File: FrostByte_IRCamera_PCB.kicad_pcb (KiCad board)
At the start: 2 copper layers, 43 parts, among them J1 Conn_01x04_Socket, J4 Conn_01x04_Socket, J5 Power_Input, J6 Conn_02x10, J7 Conn_01x02_Socket, Q1 SI3127DV-T1-GE3, SW1 SW_Push, SW2 SW_Push, U1 AP63203WU-7, U2 ESP32-S3-WROOM-1, Y2 32.768kHz

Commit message: Schematic + Layout Review Ready First Rev
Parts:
- removed D5: LED_Blue, LED_SMD:LED_0805_2012Metric_Pad1.15x1.40mm_HandSolder
- removed D6: LED_Green, LED_SMD:LED_0805_2012Metric_Pad1.15x1.40mm_HandSolder
- removed J6: Conn_02x10, Connector_PinHeader_2.54mm:PinHeader_2x10_P2.54mm_Vertical
- removed J7: Conn_01x02_Socket, TerminalBlock:TerminalBlock_Xinya_XY308-2.54-2P_1x02_P2.54mm_Horizontal
- removed L2: 6.8uH, footprints:IND_VLS6045EX-6R8M
- removed Y2: 32.768kHz, footprints:XTAL_FC-135R_32.7680KA-AG0
- added 2V8: TestPoint, TestPoint:TestPoint_THTPad_1.5x1.5mm_Drill0.7mm, F.Cu at (146.5, 132.5)
- added 3.3V: TestPoint, TestPoint:TestPoint_THTPad_1.5x1.5mm_Drill0.7mm, F.Cu at (150.5, 132.5)
- added C1: 47uF, Capacitor_THT:CP_Radial_D5.0mm_P2.00mm, F.Cu at (193.5, 129.5)
- added C12: 8pF, Capacitor_SMD:C_0805_2012Metric_Pad1.18x1.45mm_HandSolder, F.Cu at (160.5, 99.0)
- added C13: 22uF, Capacitor_SMD:C_1206_3216Metric_Pad1.33x1.80mm_HandSolder, F.Cu at (163.0, 86.0)
- added C16: 0.1uF, Capacitor_SMD:C_0805_2012Metric_Pad1.18x1.45mm_HandSolder, F.Cu at (176.5, 125.5)
- added CLK: TestPoint, TestPoint:TestPoint_THTPad_1.5x1.5mm_Drill0.7mm, F.Cu at (151.0, 115.5)
- added CS: TestPoint, TestPoint:TestPoint_THTPad_1.5x1.5mm_Drill0.7mm, F.Cu at (156.5, 115.5)
- added D2: LED_Red, LED_SMD:LED_0805_2012Metric_Pad1.15x1.40mm_HandSolder, F.Cu at (191.5, 139.0)
- added D3: LED_Blue, LED_SMD:LED_0805_2012Metric_Pad1.15x1.40mm_HandSolder, F.Cu at (196.0, 98.5)
- added GND: TestPoint, TestPoint:TestPoint_THTPad_1.5x1.5mm_Drill0.7mm, F.Cu at (154.5, 132.5)
- added J2: Conn_01x02_Socket, TerminalBlock:TerminalBlock_Xinya_XY308-2.54-2P_1x02_P2.54mm_Horizontal, F.Cu at (148.0, 88.0)
- added J3: Conn_01x04_Socket, Connector_JST:JST_SH_BM04B-SRSS-TB_1x04-1MP_P1.00mm_Vertical, F.Cu at (150.5, 139.5)
- added L1: 3.9uH, footprints:IND_VLS6045EX-6R8M, F.Cu at (185.5, 118.5)
- added MISO: TestPoint, TestPoint:TestPoint_THTPad_1.5x1.5mm_Drill0.7mm, F.Cu at (156.5, 121.5)
- added MOSI: TestPoint, TestPoint:TestPoint_THTPad_1.5x1.5mm_Drill0.7mm, F.Cu at (151.0, 121.5)
- added R10: 47, Resistor_SMD:R_0805_2012Metric_Pad1.20x1.40mm_HandSolder, F.Cu at (200.5, 98.5)
- added R14: 33, Resistor_SMD:R_0805_2012Metric_Pad1.20x1.40mm_HandSolder, F.Cu at (165.0, 112.0)
- added R2: 10k 1%, Resistor_SMD:R_0805_2012Metric_Pad1.20x1.40mm_HandSolder, F.Cu at (144.5, 95.5)
- added R5: 10k, Resistor_SMD:R_0805_2012Metric_Pad1.20x1.40mm_HandSolder, F.Cu at (167.5, 130.5)
- added R6: 2.2k, Resistor_SMD:R_0805_2012Metric_Pad1.20x1.40mm_HandSolder, F.Cu at (167.0, 106.5)
- added R9: 10k, Resistor_SMD:R_0805_2012Metric_Pad1.20x1.40mm_HandSolder, F.Cu at (188.0, 108.0)
- added RX: TestPoint, TestPoint:TestPoint_THTPad_1.5x1.5mm_Drill0.7mm, F.Cu at (196.0, 89.0)
- added SCL: TestPoint, TestPoint:TestPoint_THTPad_1.5x1.5mm_Drill0.7mm, F.Cu at (151.0, 107.0)
- added SDA: TestPoint, TestPoint:TestPoint_THTPad_1.5x1.5mm_Drill0.7mm, F.Cu at (151.0, 102.5)
- added TX: TestPoint, TestPoint:TestPoint_THTPad_1.5x1.5mm_Drill0.7mm, F.Cu at (200.5, 89.0)
- added U3: SN74AXC4T245PWR, footprints:SOP65P640X120-16N, F.Cu at (175.5, 117.5)
- added Y1: 32.768kHz, footprints:XTAL_FC-135R_32.7680KA-AG0, F.Cu at (165.5, 96.8)
- C10: value 2.2uF -> 0.1uF
- C11: value 0.1uF -> 8pF
- C14, C15, C8: value 22uF -> 0.1uF; footprint Capacitor_SMD:C_1206_3216Metric_Pad1.33x1.80mm_HandSolder -> Capacitor_SMD:C_0805_2012Metric_Pad1.18x1.45mm_HandSolder
- C2: value 0.1uF -> 2.2uF
- C4: value 47uF -> 22uF; footprint Capacitor_THT:CP_Radial_D5.0mm_P2.00mm -> Capacitor_SMD:C_1206_3216Metric_Pad1.33x1.80mm_HandSolder
- C5: value 8pF -> 22uF; footprint Capacitor_SMD:C_0805_2012Metric_Pad1.18x1.45mm_HandSolder -> Capacitor_SMD:C_1206_3216Metric_Pad1.33x1.80mm_HandSolder
- C7: value 8pF -> 1uF
- D1: value SMAJ30A -> SMAJ33A
- D4: value LED_Red -> LED_Green
- J1: value Conn_01x04_Socket -> Power_Input; footprint Connector_PinSocket_2.54mm:PinSocket_1x04_P2.54mm_Vertical -> TerminalBlock:TerminalBlock_Xinya_XY308-2.54-2P_1x02_P2.54mm_Horizontal
- J4: value Conn_01x04_Socket -> Conn_02x10; footprint Connector_JST:JST_SH_BM04B-SRSS-TB_1x04-1MP_P1.00mm_Vertical -> Connector_PinHeader_2.54mm:PinHeader_2x10_P2.54mm_Vertical
- J5: value Power_Input -> Conn_01x04_Socket; footprint TerminalBlock:TerminalBlock_Xinya_XY308-2.54-2P_1x02_P2.54mm_Horizontal -> Connector_PinSocket_2.54mm:PinSocket_1x04_P2.54mm_Vertical
- R1: value 10k -> 100k
- R11: value 270 -> 150
- R12: value 47 -> 22
- R13: value 150 -> 22
- R4: value 100k -> 2.2k
- R7: value 10k 1% -> 22
- R8: value 10k -> 270
- moved J4 80.1 mm to (136.0, 102.4), turned to 0 degrees
- moved J1 67.8 mm to (215.5, 129.0)
- moved C6 48.0 mm to (149.0, 95.5)
- moved G*** 47.5 mm to (206.0, 106.0)
- moved C11 47.0 mm to (160.5, 94.5), turned to 0 degrees
- moved C14 42.7 mm to (168.0, 86.0), turned to 180 degrees
- moved C5 41.9 mm to (182.5, 126.0), turned to -90 degrees
- moved R1 41.1 mm to (208.5, 122.5), turned to 180 degrees
- moved J5 40.1 mm to (207.0, 90.4), turned to 0 degrees
- moved C15 40.1 mm to (172.5, 125.5), turned to -90 degrees
- moved R8 38.8 mm to (186.0, 139.0), turned to 0 degrees
- moved C9 38.2 mm to (172.5, 130.5), turned to -90 degrees
- moved R13 37.4 mm to (165.0, 116.0), turned to 0 degrees
- moved R12 36.8 mm to (165.0, 120.0), turned to 0 degrees
- moved R4 36.3 mm to (171.5, 108.0), turned to 90 degrees
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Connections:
- C10 pad 1: Net-(U1-EN) -> GND
- C10 pad 2: GND -> Net-(U2-EN)
- C11 pad 1: Net-(U1-BST) -> GND
- C11 pad 2: Net-(U1-SW) -> Net-(U2-IO15)
- C2 pad 1: GND -> Net-(U1-EN)
- C2 pad 2: Net-(U2-EN) -> GND
- C3 pad 1: GND -> Net-(U1-BST)
- C3 pad 2: Net-(U2-IO0) -> Net-(U1-SW)
- C4 pad 1: Net-(U1-EN) -> +3.3V
- C5 pad 1: GND -> +3.3V
- C5 pad 2: Net-(U2-IO15) -> GND
- C7 pad 1: GND -> +3.3V
- C7 pad 2: Net-(U2-IO16) -> GND
- C8 pad 1: +3.3V -> +2V8
- C9 pad 1: +3.3V -> GND
- C9 pad 2: GND -> Net-(U2-IO0)
- D4 pad 1: GND -> /MCU/LED_2
- F1 pad 1: LINE -> Net-(J1-Pin_1)
- J1 pad 1: +3.3V -> Net-(J1-Pin_1)
- J1 pad 2: /MCU/TX -> GND
- J4 pad 1: /Peripherals/SCL -> GND
- J4 pad 2: /Peripherals/SDA -> +3.3V
- J4 pad 3: +3.3V -> unconnected-(J4-Pin_3-Pad3)
- J4 pad 4: GND -> unconnected-(J4-Pin_4-Pad4)
- J5 pad 1: LINE -> +3.3V
- J5 pad 2: GND -> /MCU/TX
- R1 pad 1: +3.3V -> GND
- R1 pad 2: /Peripherals/SCL -> Net-(Q1-Pad3)
- R12 pad 1: +3.3V -> /MCU/SPI_CS
- R13 pad 1: +3.3V -> /MCU/SPI_MOSI
- R3 pad 1: Net-(U2-EN) -> Net-(J4-Pin_20)
- R3 pad 2: +3.3V -> +2V8
- R4 pad 1: GND -> +2V8
- R4 pad 2: Net-(Q1-Pad3) -> /Peripherals/SCL
- R7 pad 1: +3.3V -> Net-(U2-IO13)
- R7 pad 2: /MCU/CAM_TEMP -> /MCU/SPI_MISO
- R8 pad 2: /Peripherals/SDA -> Net-(D2-A)
- SW1 pad 2: Net-(U2-EN) -> Net-(U2-IO0)
- SW2 pad 2: Net-(U2-IO0) -> Net-(U2-EN)
- U2 pad 18: /MCU/SPI_CS -> /MCU/SPI_CS_3v3
- U2 pad 19: /MCU/SPI_MOSI -> /MCU/SPI_MOSI_3v3
- U2 pad 20: /MCU/SPI_CLK -> /MCU/SPI_CLK_3v3
- U2 pad 21: /MCU/SPI_MISO -> Net-(U2-IO13)
- U2 pad 23: unconnected-(U2-IO21-Pad23) -> /MCU/VSYNC
- U2 pad 25: /MCU/CAM_TEMP -> unconnected-(U2-IO48-Pad25)
- U2 pad 26: unconnected-(U2-IO45-Pad26) -> /MCU/RESET_L_3v3
- U2 pad 33: /MCU/VSYNC -> unconnected-(U2-IO40-Pad33)
- U2 pad 34: /MCU/RESET_L -> unconnected-(U2-IO41-Pad34)
- U2 pad 35: /MCU/PW_DWN_L -> unconnected-(U2-IO42-Pad35)
- U2 pad 4: unconnected-(U2-IO4-Pad4) -> /MCU/CAM_TEMP
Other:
- copper layers 2 -> 4
- board text added: "IR Camera Interface PCB Domenic Hampson"

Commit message: rev 2 added usb prog and i2c level shifting
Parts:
- added D5: 15V, footprints:DIOM5226X240N, F.Cu at (208.5, 117.5)
- moved G*** 1.00 mm to (206.0, 107.0)
- moved J5 0.50 mm to (206.5, 90.4)
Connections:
- D1 pad 1: Net-(D1-A1) -> /Power_Circuitry/source
- F1 pad 2: Net-(D1-A1) -> /Power_Circuitry/source
- J4 pad 10: /MCU/SPI_CS -> /MCU/SPI_MISO
- J4 pad 11: unconnected-(J4-Pin_11-Pad11) -> /MCU/SPI_MOSI
- J4 pad 12: /MCU/SPI_MISO -> /MCU/SPI_CS
- J4 pad 13: unconnected-(J4-Pin_13-Pad13) -> /MCU/SPI_CLK
- J4 pad 14: unconnected-(J4-Pin_14-Pad14) -> /Peripherals/SCL
- J4 pad 15: /MCU/VSYNC -> /Peripherals/SDA
- J4 pad 16: unconnected-(J4-Pin_16-Pad16) -> +2V8
- J4 pad 17: /MCU/RESET_L -> unconnected-(J4-Pin_17-Pad17)
- J4 pad 2: +3.3V -> Net-(J4-Pin_2)
- J4 pad 20: Net-(J4-Pin_20) -> +3.3V
- J4 pad 3: unconnected-(J4-Pin_3-Pad3) -> /MCU/RESET_L
- J4 pad 5: /Peripherals/SDA -> /MCU/VSYNC
- J4 pad 6: +2V8 -> unconnected-(J4-Pin_6-Pad6)
- J4 pad 7: /MCU/SPI_CLK -> unconnected-(J4-Pin_7-Pad7)
- J4 pad 8: /Peripherals/SCL -> unconnected-(J4-Pin_8-Pad8)
- J4 pad 9: /MCU/SPI_MOSI -> unconnected-(J4-Pin_9-Pad9)
- Q1 pad 1: Net-(D1-A1) -> /Power_Circuitry/source
- Q1 pad 2: unconnected-(Q1-Pad2) -> /Power_Circuitry/source
- Q1 pad 5: unconnected-(Q1-Pad5) -> /Power_Circuitry/source
- Q1 pad 6: unconnected-(Q1-Pad6) -> /Power_Circuitry/source
- R3 pad 1: Net-(J4-Pin_20) -> Net-(J4-Pin_2)
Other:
- board text added: "3V3"
- board text added: "3v3"
- board text added: "GND"
- board text removed: "1 (needs to be here)"

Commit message: minor fixes and updated PCB layout
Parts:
- removed 2V8, 3.3V: TestPoint, TestPoint:TestPoint_THTPad_1.5x1.5mm_Drill0.7mm
- removed the G*** at (206.0, 107.0)
- added 2v8: TestPoint, TestPoint:TestPoint_THTPad_1.5x1.5mm_Drill0.7mm, F.Cu at (197.0, 141.0)
- added 3v3: TestPoint, TestPoint:TestPoint_THTPad_1.5x1.5mm_Drill0.7mm, F.Cu at (202.0, 141.0)
- added C17: 0.1uF, Capacitor_SMD:C_0805_2012Metric_Pad1.18x1.45mm_HandSolder, F.Cu at (153.0, 109.0)
- added C18: 0.1uF, Capacitor_SMD:C_0805_2012Metric_Pad1.18x1.45mm_HandSolder, F.Cu at (167.0, 111.0)
- added C19: 0.1uF, Capacitor_SMD:C_0805_2012Metric_Pad1.18x1.45mm_HandSolder, F.Cu at (206.0, 112.0)
- added D6: SS34, footprints:DIO_SS34, F.Cu at (202.0, 106.0)
- added F2: 3A, Fuse:Fuse_0603_1608Metric_Pad1.05x0.95mm_HandSolder, F.Cu at (198.0, 113.0)
- added G***: LOGO, footprints:Small_Logo, F.Cu at (152.0, 116.0)
- added J6: GSB1C41110SSHR, footprints:AMPHENOL_GSB1C41110SSHR, F.Cu at (218.6, 101.1)
- added R15: 22, Resistor_SMD:R_0805_2012Metric_Pad1.20x1.40mm_HandSolder, F.Cu at (211.0, 103.0)
- added R16: 5.1k, Resistor_SMD:R_0805_2012Metric_Pad1.20x1.40mm_HandSolder, F.Cu at (211.0, 107.0)
- added R17: 10k, Resistor_SMD:R_0805_2012Metric_Pad1.20x1.40mm_HandSolder, F.Cu at (195.0, 103.0)
- added R18: 0, Resistor_SMD:R_0805_2012Metric_Pad1.20x1.40mm_HandSolder, F.Cu at (192.0, 109.0)
- added U4: TCA9517DGKR, footprints:SOP65P490X110-8N, F.Cu at (160.0, 109.0)
- C13: value 22uF -> DNP
- J3: footprint Connector_JST:JST_SH_BM04B-SRSS-TB_1x04-1MP_P1.00mm_Vertical -> footprints:CONN4_BM04B-SRSS_JST
- J5: value Conn_01x04_Socket -> UART; footprint Connector_PinSocket_2.54mm:PinSocket_1x04_P2.54mm_Vertical -> footprints:CONN4_BM04B-SRSS_JST
- moved GND 53.2 mm to (207.0, 141.0)
- moved R7 30.8 mm to (211.0, 99.0), turned to 180 degrees
- moved CLK 19.7 mm to (142.0, 133.0)
- moved CS 18.7 mm to (150.0, 133.0)
- moved MOSI 12.5 mm to (146.0, 133.0)
- moved MISO 11.8 mm to (154.0, 133.0)
- moved SCL 11.4 mm to (154.0, 96.0)
- moved RX 5.39 mm to (201.0, 87.0)
- moved R12 4.12 mm to (166.0, 124.0)
- moved R13 4.12 mm to (166.0, 120.0)
- moved R14 4.12 mm to (166.0, 116.0)
- moved TX 4.03 mm to (197.0, 87.0)
- moved SDA 3.35 mm to (154.0, 101.0)
- moved R6 1.50 mm to (167.0, 105.0)
- moved U3 1.50 mm to (175.5, 119.0)
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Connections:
- C9 pad 2: Net-(U2-IO0) -> Net-(C9-Pad2)
- D5 pad 1: Net-(D5-K) -> /Power_Circuitry/source
- D5 pad 2: /Power_Circuitry/source -> Net-(D5-A)
- J3 pad 1: /Peripherals/SCL -> /MCU/SCL_A
- J3 pad 2: /Peripherals/SDA -> /MCU/SDA_A
- J4 pad 14: /Peripherals/SCL -> /MCU/SCL_B
- J4 pad 15: /Peripherals/SDA -> /MCU/SDA_B
- J5 pad 1: +3.3V -> +5V
- J5 pad 2: /MCU/TX -> /MCU/RX
- J5 pad 3: /MCU/RX -> /MCU/TX
- Q1 pad 3: Net-(D5-K) -> Net-(D5-A)
- R1 pad 2: Net-(D5-K) -> Net-(D5-A)
- R4 pad 1: +2V8 -> +3.3V
- R4 pad 2: /Peripherals/SCL -> /MCU/SCL_A
- R6 pad 1: +2V8 -> +3.3V
- R6 pad 2: /Peripherals/SDA -> /MCU/SDA_A
- R7 pad 1: Net-(U2-IO13) -> Net-(J6-DN1)
- R7 pad 2: /MCU/SPI_MISO -> /MCU/USB_D-
- SCL pad 1: /Peripherals/SCL -> /MCU/SCL_A
- SDA pad 1: /Peripherals/SDA -> /MCU/SDA_A
- SW1 pad 2: Net-(U2-IO0) -> Net-(C9-Pad2)
- U2 pad 12: /Peripherals/SDA -> /MCU/SDA_A
- U2 pad 13: unconnected-(U2-IO19-Pad13) -> /MCU/USB_D-
- U2 pad 14: unconnected-(U2-IO20-Pad14) -> /MCU/USB_D+
- U2 pad 17: /Peripherals/SCL -> /MCU/SCL_A
- U2 pad 21: Net-(U2-IO13) -> /MCU/SPI_MISO
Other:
- board text removed: "3V3"

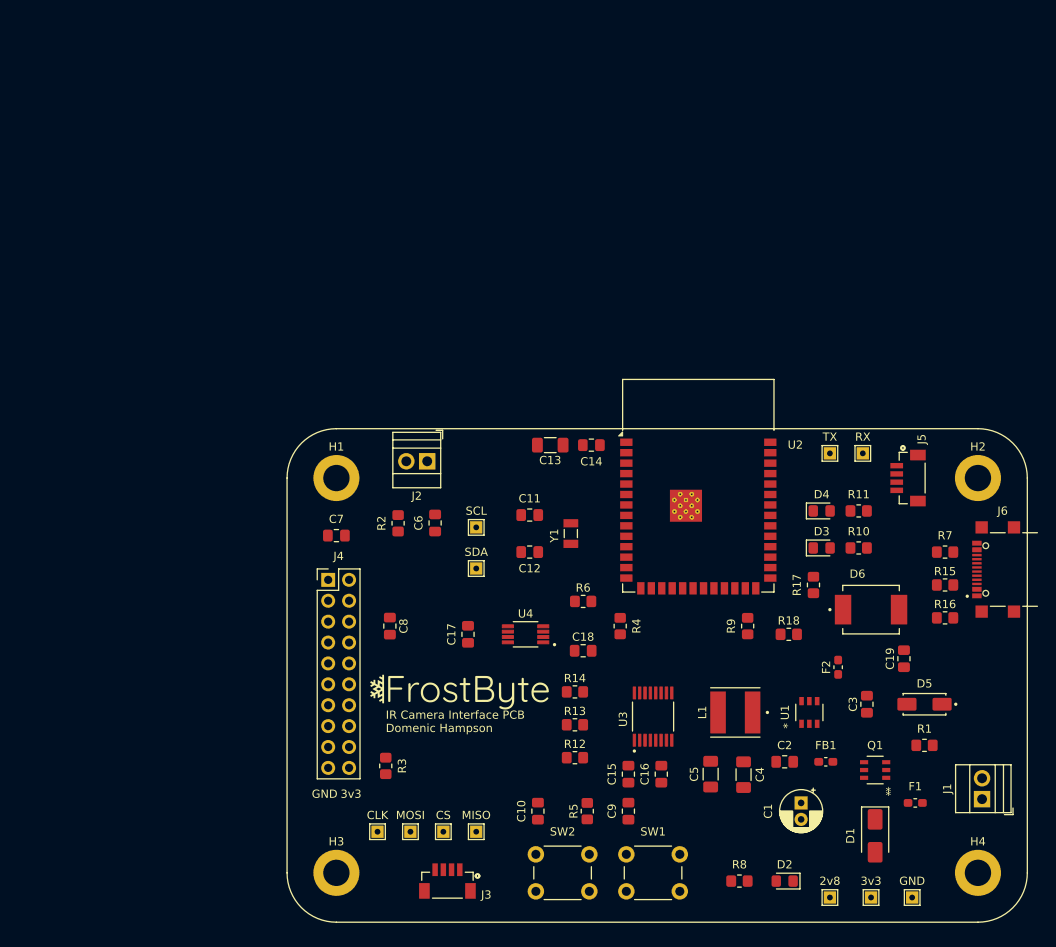
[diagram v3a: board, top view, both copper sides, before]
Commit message: Updated Schematic and fixed some routing issues
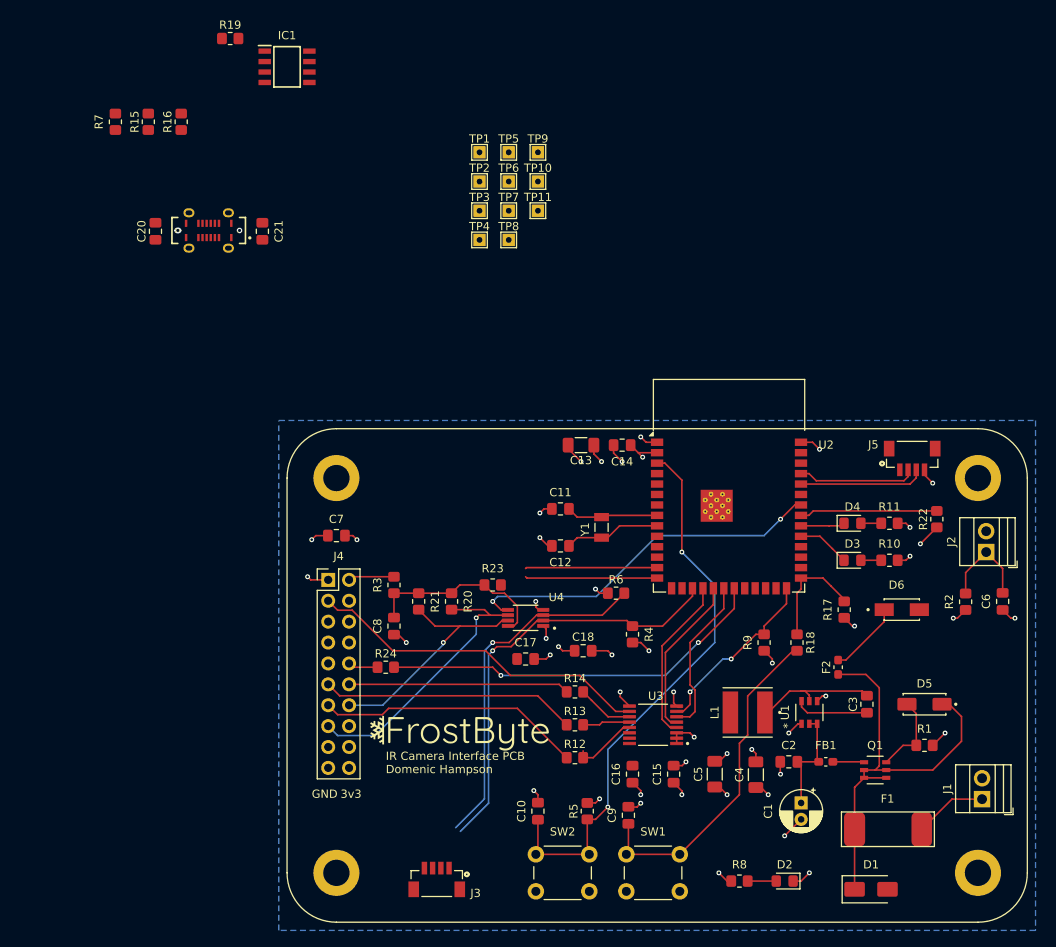
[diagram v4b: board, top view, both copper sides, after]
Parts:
- removed 2v8, 3v3, CLK, CS, GND, MISO, MOSI, RX, SCL, SDA, TX: TestPoint, TestPoint:TestPoint_THTPad_1.5x1.5mm_Drill0.7mm
- removed C19: 0.1uF, Capacitor_SMD:C_0805_2012Metric_Pad1.18x1.45mm_HandSolder
- added C20: 0.1uF, Capacitor_SMD:C_0805_2012Metric_Pad1.18x1.45mm_HandSolder, F.Cu at (115.0, 60.0)
- added C21: 0.1uF, Capacitor_SMD:C_0805_2012Metric_Pad1.18x1.45mm_HandSolder, F.Cu at (128.0, 60.0)
- added IC1: USB6B1RL, footprints:SOIC127P600X175-8N, F.Cu at (131.0, 40.0)
- added R19: 5.1k, Resistor_SMD:R_0805_2012Metric_Pad1.20x1.40mm_HandSolder, F.Cu at (124.1, 36.6)
- added R20: 2.2k, Resistor_SMD:R_0805_2012Metric_Pad1.20x1.40mm_HandSolder, F.Cu at (151.0, 105.0)
- added R21: 2.2k, Resistor_SMD:R_0805_2012Metric_Pad1.20x1.40mm_HandSolder, F.Cu at (147.0, 105.0)
- added R22: 10k, Resistor_SMD:R_0805_2012Metric_Pad1.20x1.40mm_HandSolder, F.Cu at (210.0, 95.0)
- added R23: 10k, Resistor_SMD:R_0805_2012Metric_Pad1.20x1.40mm_HandSolder, F.Cu at (156.0, 103.0)
- added R24: 22, Resistor_SMD:R_0805_2012Metric_Pad1.20x1.40mm_HandSolder, F.Cu at (143.0, 113.0)
- added TP1: TestPoint, TestPoint:TestPoint_THTPad_1.5x1.5mm_Drill0.7mm, F.Cu at (154.4, 50.4)
- added TP10: TestPoint, TestPoint:TestPoint_THTPad_1.5x1.5mm_Drill0.7mm, F.Cu at (161.5, 54.0)
- added TP11: TestPoint, TestPoint:TestPoint_THTPad_1.5x1.5mm_Drill0.7mm, F.Cu at (161.5, 57.5)
- added TP2: TestPoint, TestPoint:TestPoint_THTPad_1.5x1.5mm_Drill0.7mm, F.Cu at (154.4, 54.0)
- added TP3: TestPoint, TestPoint:TestPoint_THTPad_1.5x1.5mm_Drill0.7mm, F.Cu at (154.4, 57.5)
- added TP4: TestPoint, TestPoint:TestPoint_THTPad_1.5x1.5mm_Drill0.7mm, F.Cu at (154.4, 61.0)
- added TP5: TestPoint, TestPoint:TestPoint_THTPad_1.5x1.5mm_Drill0.7mm, F.Cu at (157.9, 50.4)
- added TP6: TestPoint, TestPoint:TestPoint_THTPad_1.5x1.5mm_Drill0.7mm, F.Cu at (157.9, 54.0)
- added TP7: TestPoint, TestPoint:TestPoint_THTPad_1.5x1.5mm_Drill0.7mm, F.Cu at (157.9, 57.5)
- added TP8: TestPoint, TestPoint:TestPoint_THTPad_1.5x1.5mm_Drill0.7mm, F.Cu at (157.9, 61.0)
- added TP9: TestPoint, TestPoint:TestPoint_THTPad_1.5x1.5mm_Drill0.7mm, F.Cu at (161.5, 50.4)
- D6: value SS34 -> B240A-13-F; footprint footprints:DIO_SS34 -> footprints:DIOM5226X230N
- F1: value SF-0603S063-2 -> 3404.2413.11; footprint Fuse:Fuse_0603_1608Metric_Pad1.05x0.95mm_HandSolder -> footprints:Small_SMD_Fuse_Holder
- F2: value 3A -> 1A Slow Blow
- J6: value GSB1C41110SSHR -> USB4120-03-C_REVA6; footprint footprints:AMPHENOL_GSB1C41110SSHR -> footprints:GCT_USB4120-03-C_REVA6
- moved R7 113.6 mm to (110.1, 46.7), turned to -90 degrees
- moved R15 112.0 mm to (114.1, 46.7), turned to 90 degrees
- moved R16 110.7 mm to (118.1, 46.7), turned to 90 degrees
- moved J6 105.5 mm to (121.5, 59.9), turned to 180 degrees
- moved C6 69.7 mm to (218.0, 105.0)
- moved R2 69.7 mm to (213.5, 105.0)
- moved J2 68.9 mm to (216.0, 99.0), turned to 90 degrees
- moved R3 22.0 mm to (144.0, 103.0), turned to -90 degrees
- moved C17 7.62 mm to (160.0, 112.0), turned to 0 degrees
- moved D1 6.52 mm to (202.0, 140.0), turned to 0 degrees
- moved F1 5.62 mm to (204.0, 134.0)
- moved C15 5.50 mm to (178.0, 126.0)
- moved G*** 5.00 mm to (152.0, 121.0)
- moved R17 4.79 mm to (198.7, 106.0)
- moved R6 4.12 mm to (171.0, 104.0)
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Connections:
- D6 pad A: (no net) -> +5V
- D6 pad C: (no net) -> Net-(D6-PadC)
- F2 pad 2: Net-(D6-K) -> Net-(D6-PadC)
- J4 pad 10: /MCU/SPI_MISO -> Net-(J4-Pin_10)
- J5 pad 2: /MCU/RX -> /MCU/TX
- J5 pad 3: /MCU/TX -> /MCU/RX
- J6 pad A6: Net-(J6-DP1) -> /Peripherals/D+
- J6 pad A7: Net-(J6-DN1) -> /Peripherals/D-
- J6 pad B5: unconnected-(J6-CC2-PadB5) -> Net-(J6-CC2)
- J6 pad B6: unconnected-(J6-DP2-PadB6) -> /Peripherals/D+
- J6 pad B7: unconnected-(J6-DN2-PadB7) -> /Peripherals/D-
- R12 pad 1: /MCU/SPI_CS -> /MCU/SPI_CLK
- R14 pad 1: /MCU/SPI_CLK -> /MCU/SPI_CS
- R15 pad 1: /MCU/USB_D+ -> /MCU/USB_D-
- R15 pad 2: Net-(J6-DP1) -> /Peripherals/D-
- R16 pad 2: Net-(J6-CC1) -> Net-(J6-CC2)
- R7 pad 1: Net-(J6-DN1) -> /Peripherals/D+
- R7 pad 2: /MCU/USB_D- -> /MCU/USB_D+
- U2 pad 10: unconnected-(U2-IO17-Pad10) -> Net-(U2-IO17)
- U2 pad 33: unconnected-(U2-IO40-Pad33) -> /MCU/EN_SPI
- U2 pad 34: unconnected-(U2-IO41-Pad34) -> /MCU/EN_I2C
- U3 pad 14: GND -> /MCU/EN_SPI
- U3 pad 15: GND -> /MCU/EN_SPI
- U4 pad 5: +3.3V -> /MCU/EN_I2C
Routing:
- net Net-(U2-EN): track 0.00 -> 68.9 mm, vias 0 -> 2
- net GND: track 0.00 -> 55.8 mm, vias 0 -> 27
- net /Power_Circuitry/source: track 0.00 -> 52.8 mm
- net /MCU/SCL_A: track 0.00 -> 52.1 mm, vias 0 -> 1
- net /MCU/SPI_MISO: track 0.00 -> 47.6 mm, vias 0 -> 2
- net /MCU/EN_I2C: track 0.00 -> 44.6 mm, vias 0 -> 2
- net /MCU/SDA_A: track 0.00 -> 42.8 mm, vias 0 -> 1
- net +3.3V: track 0.00 -> 42.7 mm, vias 0 -> 20
- net /MCU/RESET_L: track 0.00 -> 42.2 mm
- net Net-(C9-Pad2): track 0.00 -> 41.8 mm
- net /MCU/SDA_B: track 0.00 -> 34.5 mm, vias 0 -> 1
- net /MCU/SPI_CLK: track 0.00 -> 32.3 mm
- net /MCU/SPI_MOSI: track 0.00 -> 31.0 mm
- net /MCU/SCL_B: track 0.00 -> 29.7 mm, vias 0 -> 1
- net /MCU/SPI_CS: track 0.00 -> 26.8 mm
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- added copper zone on In2.Cu, net +3.3V
- added copper zone on B.Cu, net GND
- added copper zone on In1.Cu, net GND
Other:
- board outline added: 0.7 x 0.5 mm

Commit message: Layout + Schem complete, rough routing
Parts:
- moved TP1 84.0 mm to (212.0, 111.5)
- moved TP5 81.6 mm to (142.5, 130.5)
- moved TP8 81.5 mm to (142.5, 141.1)
- moved R7 81.3 mm to (171.0, 100.6), turned to 180 degrees
- moved TP7 80.5 mm to (142.5, 136.5)
- moved R15 79.8 mm to (171.0, 102.6), turned to 0 degrees
- moved TP11 77.8 mm to (217.5, 111.5)
- moved TP2 77.1 mm to (145.5, 130.5)
- moved TP6 75.3 mm to (206.5, 111.5)
- moved TP3 73.2 mm to (148.5, 130.5)
- moved TP4 69.5 mm to (151.5, 130.5)
- moved R19 63.9 mm to (155.0, 92.5), turned to -90 degrees
- moved IC1 58.8 mm to (147.2, 96.5), turned to -90 degrees
- moved TP9 54.9 mm to (200.0, 89.5)
- moved TP10 49.8 mm to (200.0, 85.5)
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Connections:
- IC1 pad 2: /Peripherals/D+ -> /Peripherals/USB_D+
- IC1 pad 3: /Peripherals/D- -> /Peripherals/USB_D-
- J6 pad A6: /Peripherals/D+ -> /Peripherals/USB_D+
- J6 pad A7: /Peripherals/D- -> /Peripherals/USB_D-
- J6 pad B6: /Peripherals/D+ -> /Peripherals/USB_D+
- J6 pad B7: /Peripherals/D- -> /Peripherals/USB_D-
- R15 pad 1: /MCU/USB_D- -> /Peripherals/USB_D-
- R15 pad 2: /Peripherals/D- -> /Peripherals/USB_D-
- R7 pad 1: /Peripherals/D+ -> /Peripherals/USB_D+
- R7 pad 2: /MCU/USB_D+ -> /Peripherals/USB_D+
- U2 pad 13: /MCU/USB_D- -> /Peripherals/USB_D-
- U2 pad 14: /MCU/USB_D+ -> /Peripherals/USB_D+
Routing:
- net /Peripherals/USB_D-: track 0.00 -> 41.7 mm, vias 0 -> 4
- net /Peripherals/USB_D+: track 0.00 -> 40.5 mm, vias 0 -> 1
- net Net-(U2-IO17): track 0.00 -> 28.8 mm, vias 0 -> 2
- net +5V: track 0.00 -> 20.3 mm
- net /MCU/SDA_A: track 42.8 -> 59.1 mm, vias 1 -> 4
- net /MCU/USB_D+: track 16.1 -> 0.00 mm
- net /MCU/USB_D-: track 16.0 -> 0.00 mm
- net GND: track 55.8 -> 69.4 mm, vias 27 -> 30
- net /MCU/RX: track 15.6 -> 26.5 mm
- net Net-(J6-CC2): track 0.00 -> 8.07 mm
- net Net-(J6-CC1): track 0.00 -> 7.72 mm
- net /MCU/SCL_A: track 52.1 -> 59.0 mm, vias 1 -> 2
- net +3.3V: track 42.7 -> 48.0 mm, vias 20 -> 23
- net /MCU/TX: track 14.5 -> 18.1 mm
- net +2V8: track 22.8 -> 19.7 mm, vias 0 -> 6
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- added copper zone on In2.Cu, net +2V8
- added copper zone on In2.Cu, net +5V
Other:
- board size 0.7 x 0.5 mm -> 91 x 62 mm
